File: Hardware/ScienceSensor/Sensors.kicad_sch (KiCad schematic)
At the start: 41 parts, among them J1 USB_A, Q2 BSS138, Q4 BSS138, U4 FT230XS

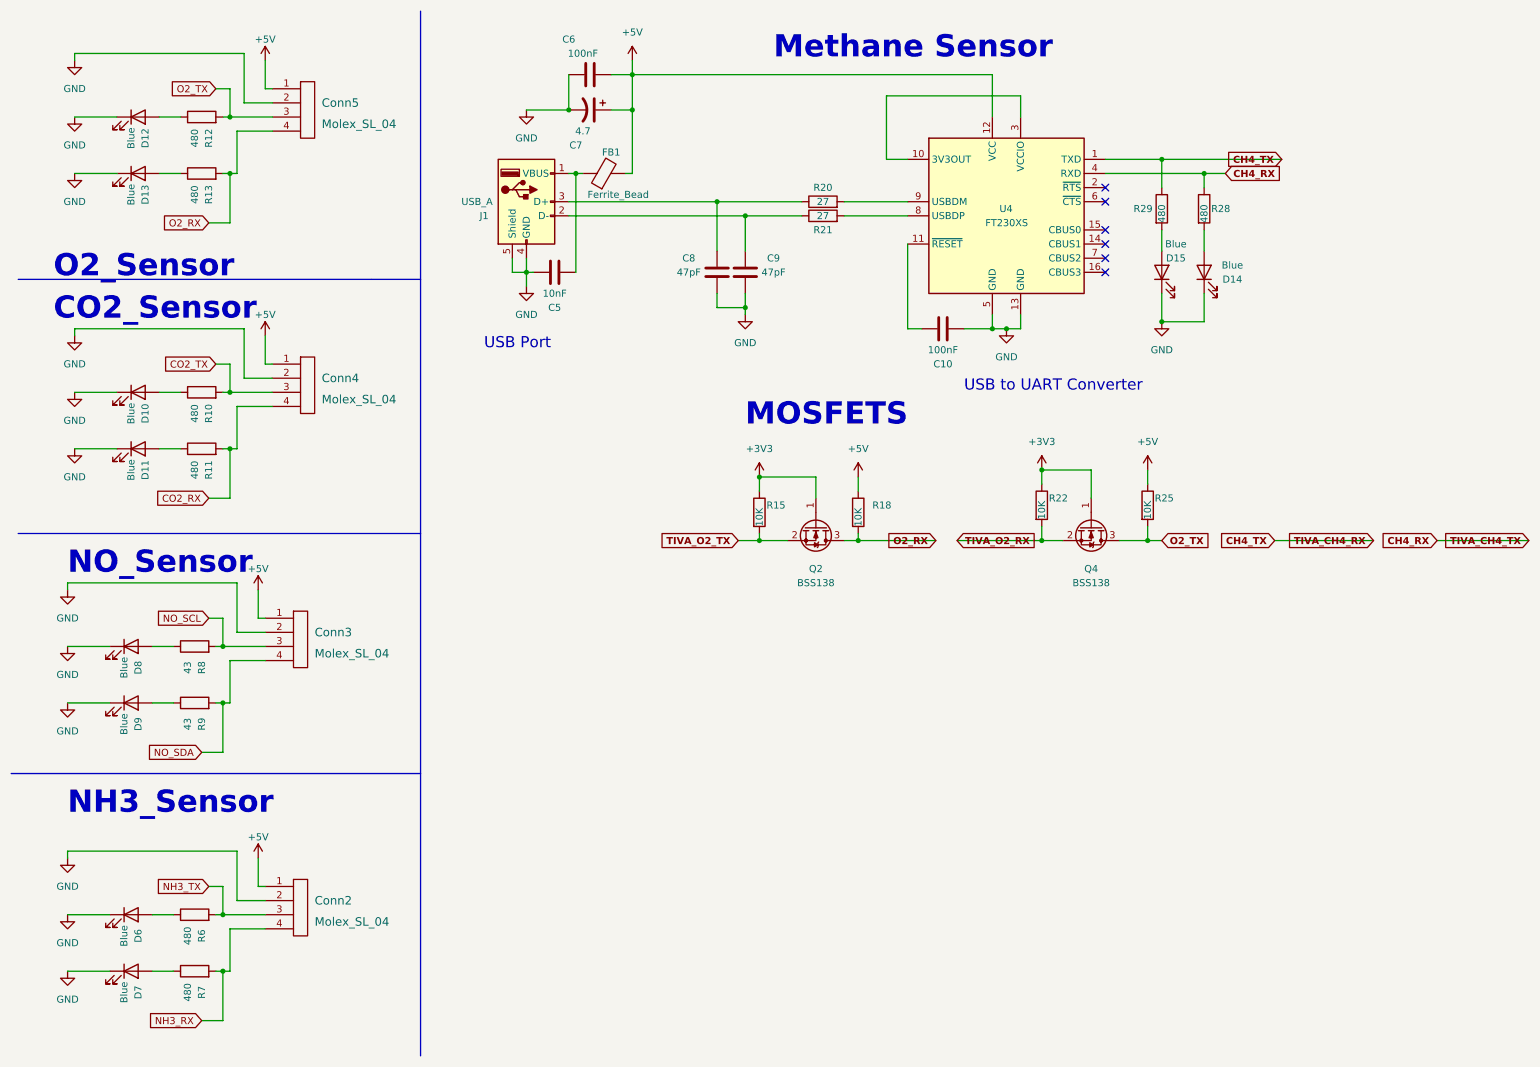
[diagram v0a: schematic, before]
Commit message: Created servo and started limit switch for microscope.
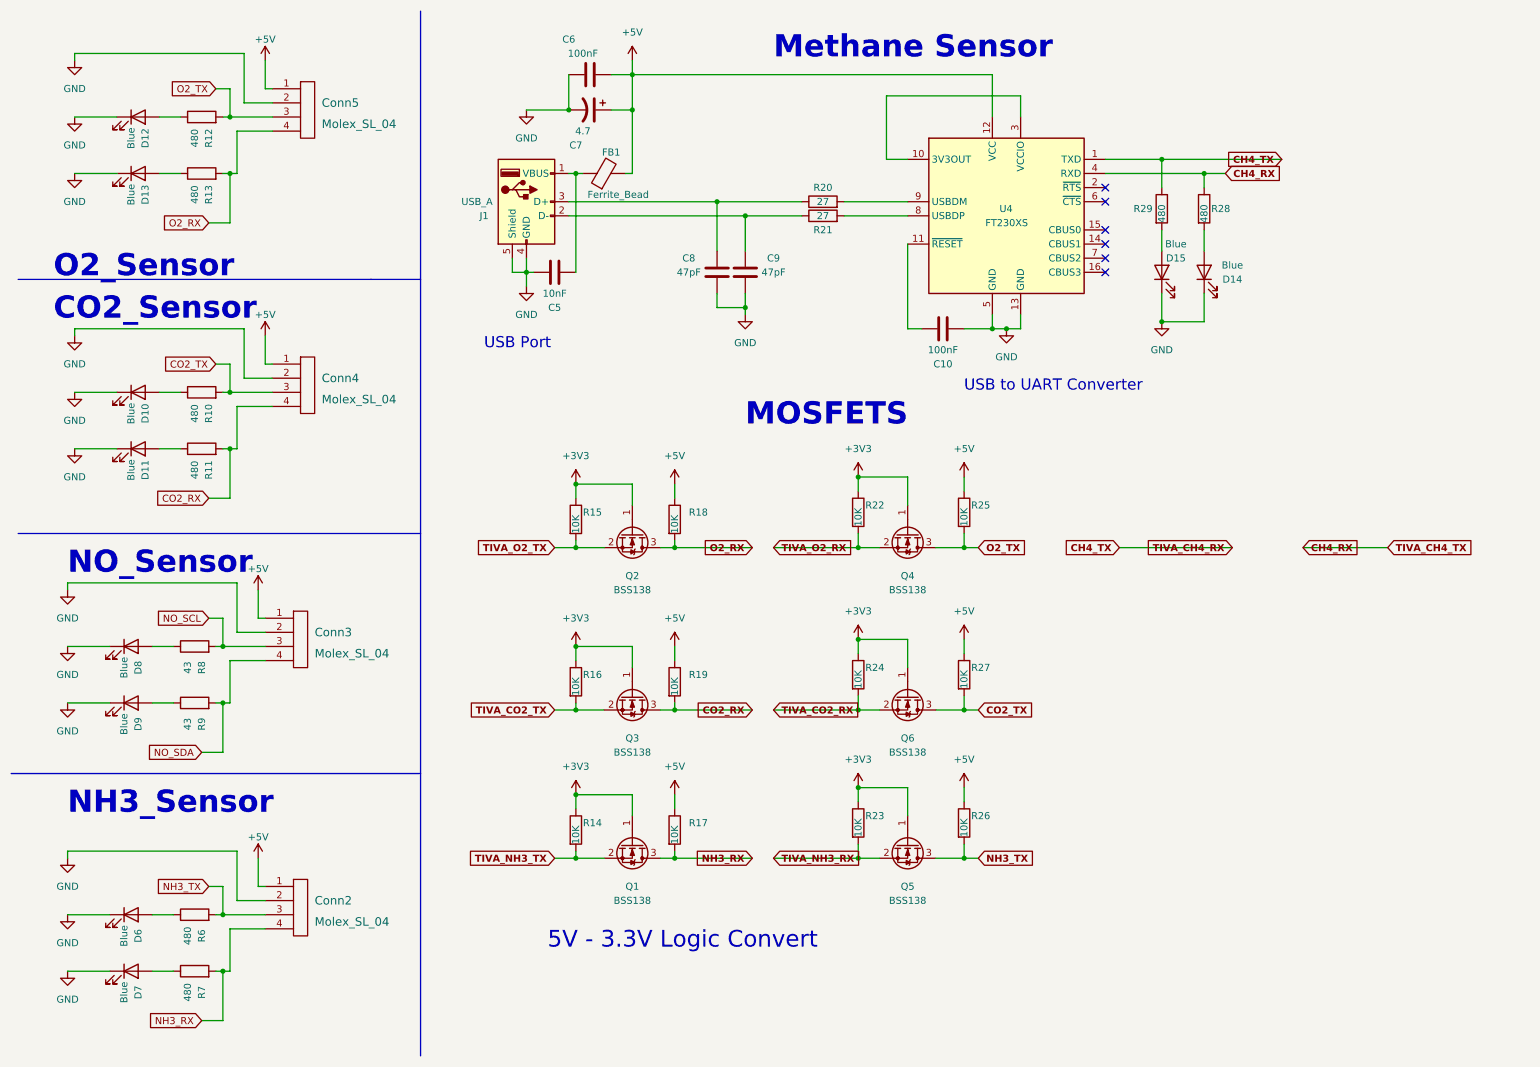
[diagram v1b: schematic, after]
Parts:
- added Q1, Q3, Q5, Q6: BSS138, symbol Device:Q_NMOS_GSD
- added R14, R16, R17, R19, R23, R24, R26, R27: 10K, symbol Device:R
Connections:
- net +3V3: now also Q1.1 (G), Q3.1 (G), Q5.1 (G), Q6.1 (G), R14.1, R16.1, R23.1, R24.1
- net +5V: now also R17.1, R19.1, R26.1, R27.1
- net CO2_RX: now also Q3.3 (D), R19.2
- net CO2_TX: now also Q6.3 (D), R27.2
- net NH3_RX: now also Q1.3 (D), R17.2
- net NH3_TX: now also Q5.3 (D), R26.2
- new net TIVA_CO2_RX: Q6.2 (S), R24.2
- new net TIVA_CO2_TX: Q3.2 (S), R16.2
- new net TIVA_NH3_RX: Q5.2 (S), R23.2
- new net TIVA_NH3_TX: Q1.2 (S), R14.2
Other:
- note added: "5V - 3.3V Logic Convert"
- moved on the sheet: Q2, Q4, R15, R18, R22, R25
